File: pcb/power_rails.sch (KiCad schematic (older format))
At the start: 26 parts

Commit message: worked on configuration
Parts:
- removed C? (x2): 4.7uF, symbol C
- removed U?: TLV702xx-DBV, symbol TLV702xx-DBV
- added C? (x2): 47uF, symbol C
- added C?: 10uF, symbol C
- added C? (x2): DNP, symbol C
- added C? (x2): 150uF, symbol CP1
- added C?: C, symbol C
- added CON?: BARREL_JACK, symbol BARREL_JACK
- added F?: FUSE, symbol FUSE
- added R?: 13.3K, symbol R
- added R?: 8.25K, symbol R
- added R?: 215K, symbol R
- added U?: LTM4622, symbol LTM4622
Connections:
- net labels added: +12V
- wire segments 90 -> 129
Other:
- note added: "Channel 1: 3.3V\nChannel 2: 5V"
- note removed: "3V3 For Misc."
- moved on the sheet: C?, R?

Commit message: schematic completed. Time for review
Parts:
- removed C?: 0.47uF, symbol C
- removed C?: 22uF, symbol C
- removed C? (x2): 4.7uF, symbol C
- removed R? (x2): 10K, symbol R
- removed U?: XRP2997, symbol XRP2997
- added FB?: FILTER, symbol FILTER
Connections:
- net labels removed: VTT
- wire segments 129 -> 109
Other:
- note removed: "DDR VTT Regulator"
- moved on the sheet: C?, U?

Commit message: Added part numbers and updated schematic
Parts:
- gave numbers to parts that had none: 31

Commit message: mostly done with component placement
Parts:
- removed C310, C311: 150uF, symbol CP1
- added C310, C311: 47uF, wbraun_smd:C_0805, symbol C
- C301, C302, C303, C312, C313, C314, C315: footprint (none) -> wbraun_smd:C_0402
- C304, C305, C306, C307, C308, C309: footprint (none) -> wbraun_smd:C_0805
- C316: value C -> 10uF; footprint (none) -> wbraun_smd:C_0805
- CON301: footprint (none) -> wbraun_smd:DC_2.1mm_PJ-202A
- F301: footprint (none) -> wbraun_smd:SMD-0805
- FB301: footprint (none) -> wbraun_smd:L_0603
- R301, R302, R303, R304, R305, R306, R307, R308: footprint (none) -> wbraun_smd:R_0402
- U301, U302: footprint (none) -> wbraun_smd:LGA25_6_25x6_25
- U303: footprint (none) -> wbraun_smd:TSOT-23-5
- U304: footprint (none) -> wbraun_smd:SOT223-5
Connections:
- net +3V3: now also C310.1
- net +5V: now also C311.1
- net GND: now also C310.2, C311.2
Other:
- note added: "10uF decoupling caps are 0805"
- note added: "47uF are 0805"

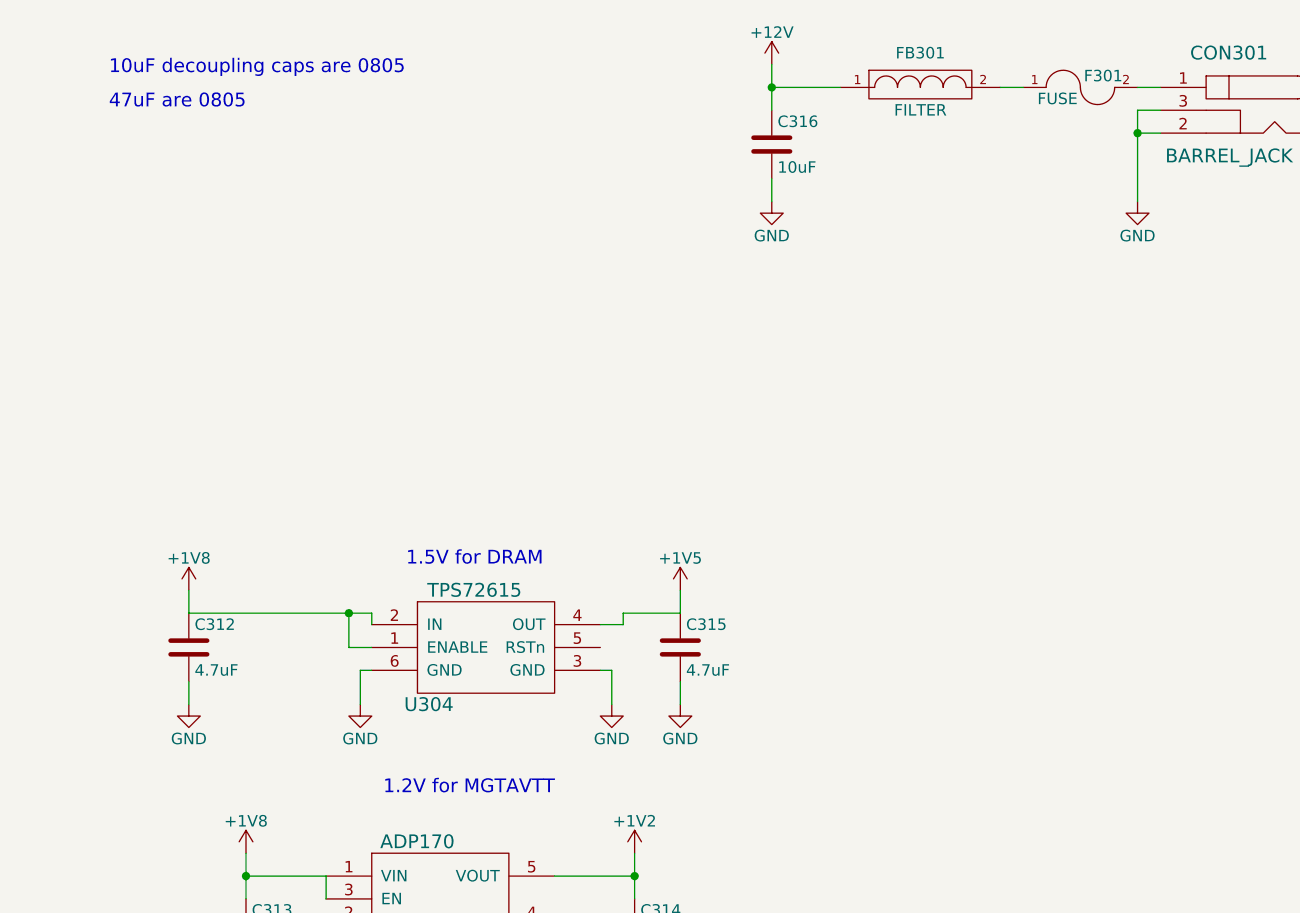
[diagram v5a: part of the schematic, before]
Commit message: Finished most of the routing, removed DDR-3
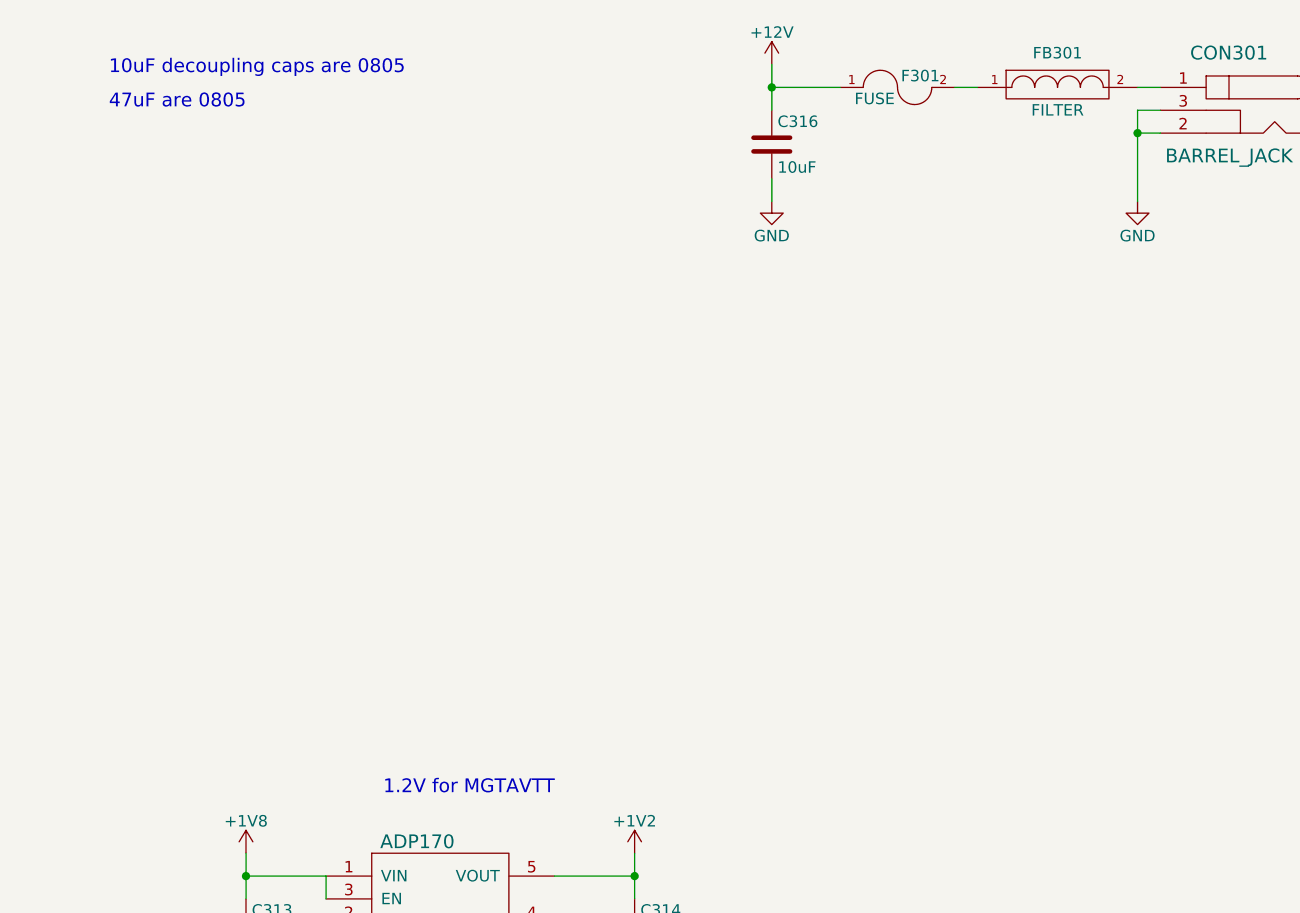
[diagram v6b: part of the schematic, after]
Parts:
- removed C312, C315: 4.7uF, wbraun_smd:C_0402, symbol C
- removed U304: TPS72615, wbraun_smd:SOT223-5, symbol TPS72615
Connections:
- net +12V: now also F301.1; no longer FB301.1
- net at CON301.1: now also FB301.2; no longer F301.2
- new net: F301.2, FB301.1
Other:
- note removed: "1.5V for DRAM"
- moved on the sheet: F301, FB301
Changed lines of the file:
@@
 $Descr A4 11693 8268
 encoding utf-8
-Sheet 3 13
+Sheet 3 11
 Title ""
 Date ""
@@
 1V @ 0.15A for MGTAVCC
 $Comp
-L TPS72615 U304
-U 1 1 561AB60E
-P 6850 3450
-F 0 "U304" H 6600 3200 60  0000 C CNN
-F 1 "TPS72615" H 6800 3700 60  0000 C CNN
-F 2 "wbraun_smd:SOT223-5" H 7450 3250 60  0001 C CNN
-F 3 "" H 7450 3250 60  0000 C CNN
-	1    6850 3450
-	1    0    0    -1
-$EndComp
-$Comp
 L ADP170 U303
 U 1 1 561AB8F7
@@
 F 3 "" H 4200 1350 60  0000 C CNN
 	1    4200 1350
-	1    0    0    -1
-$EndComp
-$Comp
-L C C312
-U 1 1 561AD736
-P 5550 3450
-F 0 "C312" H 5575 3550 50  0000 L CNN
-F 1 "4.7uF" H 5575 3350 50  0000 L CNN
-F 2 "wbraun_smd:C_0402" H 5588 3300 30  0001 C CNN
-F 3 "" H 5550 3450 60  0000 C CNN
-	1    5550 3450
-	1    0    0    -1
-$EndComp
-$Comp
-L C C315
-U 1 1 561AD79D
-P 7700 3450
-F 0 "C315" H 7725 3550 50  0000 L CNN
-F 1 "4.7uF" H 7725 3350 50  0000 L CNN
-F 2 "wbraun_smd:C_0402" H 7738 3300 30  0001 C CNN
-F 3 "" H 7700 3450 60  0000 C CNN
-	1    7700 3450
 	1    0    0    -1
 $EndComp
@@
 Wire Wire Line
 	1750 1550 1750 1600
-Text Notes 6500 3100 0    60   ~ 0
-1.5V for DRAM
-Wire Wire Line
-	6350 3450 6250 3450
 Text Label 1650 2150 2    60   ~ 0
 1V8_PGOOD
 Connection ~ 1750 2150
-Wire Wire Line
-	5550 3300 6350 3300
-Wire Wire Line
-	6350 3300 6350 3350
-$Comp
-L GND #PWR024
-U 1 1 561AF8D8
-P 5550 3700
-F 0 "#PWR024" H 5550 3450 50  0001 C CNN
-F 1 "GND" H 5550 3550 50  0000 C CNN
-F 2 "" H 5550 3700 60  0000 C CNN
-F 3 "" H 5550 3700 60  0000 C CNN
-	1    5550 3700
-	1    0    0    -1
-$EndComp
-$Comp
-L GND #PWR025
-U 1 1 561AF912
-P 6300 3700
-F 0 "#PWR025" H 6300 3450 50  0001 C CNN
-F 1 "GND" H 6300 3550 50  0000 C CNN
-F 2 "" H 6300 3700 60  0000 C CNN
-F 3 "" H 6300 3700 60  0000 C CNN
-	1    6300 3700
-	1    0    0    -1
-$EndComp
-$Comp
-L GND #PWR026
-U 1 1 561AF94C
-P 7400 3700
-F 0 "#PWR026" H 7400 3450 50  0001 C CNN
-F 1 "GND" H 7400 3550 50  0000 C CNN
-F 2 "" H 7400 3700 60  0000 C CNN
-F 3 "" H 7400 3700 60  0000 C CNN
-	1    7400 3700
-	1    0    0    -1
-$EndComp
-Wire Wire Line
-	6350 3550 6300 3550
-Wire Wire Line
-	6300 3550 6300 3700
-Wire Wire Line
-	5550 3600 5550 3700
-Wire Wire Line
-	7350 3350 7450 3350
-Wire Wire Line
-	7450 3350 7450 3300
-Wire Wire Line
-	7450 3300 7700 3300
-Wire Wire Line
-	7350 3550 7400 3550
-Wire Wire Line
-	7400 3550 7400 3700
-$Comp
-L GND #PWR027
-U 1 1 561AFACB
-P 7700 3700
-F 0 "#PWR027" H 7700 3450 50  0001 C CNN
-F 1 "GND" H 7700 3550 50  0000 C CNN
-F 2 "" H 7700 3700 60  0000 C CNN
-F 3 "" H 7700 3700 60  0000 C CNN
-	1    7700 3700
-	1    0    0    -1
-$EndComp
-Wire Wire Line
-	7700 3600 7700 3700
-$Comp
-L +1V8 #PWR028
-U 1 1 561AFBAC
-P 5550 3200
-F 0 "#PWR028" H 5550 3050 50  0001 C CNN
-F 1 "+1V8" H 5550 3340 50  0000 C CNN
-F 2 "" H 5550 3200 60  0000 C CNN
-F 3 "" H 5550 3200 60  0000 C CNN
-	1    5550 3200
-	1    0    0    -1
-$EndComp
-$Comp
-L +1V5 #PWR029
-U 1 1 561AFBE6
-P 7700 3200
-F 0 "#PWR029" H 7700 3050 50  0001 C CNN
-F 1 "+1V5" H 7700 3340 50  0000 C CNN
-F 2 "" H 7700 3200 60  0000 C CNN
-F 3 "" H 7700 3200 60  0000 C CNN
-	1    7700 3200
-	1    0    0    -1
-$EndComp
-Wire Wire Line
-	7700 3300 7700 3200
-Wire Wire Line
-	5550 3200 5550 3300
 Text Notes 6400 4100 0    60   ~ 0
 1.2V for MGTAVTT
@@
 L FUSE F301
 U 1 1 563456FC
-P 9450 1000
-F 0 "F301" H 9550 1050 50  0000 C CNN
-F 1 "FUSE" H 9350 950 50  0000 C CNN
-F 2 "wbraun_smd:SMD-0805" H 9450 1000 60  0001 C CNN
-F 3 "" H 9450 1000 60  0000 C CNN
-	1    9450 1000
+P 8650 1000
+F 0 "F301" H 8750 1050 50  0000 C CNN
+F 1 "FUSE" H 8550 950 50  0000 C CNN
+F 2 "wbraun_smd:SMD-0805" H 8650 1000 60  0001 C CNN
+F 3 "" H 8650 1000 60  0000 C CNN
+	1    8650 1000
 	1    0    0    -1
 $EndComp
@@
 Wire Wire Line
 	8100 1400 8100 1500
-Wire Wire Line
-	6250 3450 6250 3300
-Connection ~ 6250 3300
 $Comp
 L FILTER FB301
 U 1 1 56537CA5
-P 8750 1000
-F 0 "FB301" H 8750 1150 50  0000 C CNN
-F 1 "FILTER" H 8750 900 50  0000 C CNN
-F 2 "wbraun_smd:L_0603" H 8750 1000 60  0001 C CNN
-F 3 "" H 8750 1000 60  0000 C CNN
-	1    8750 1000
-	1    0    0    -1
-$EndComp
-Wire Wire Line
-	9200 1000 9100 1000
+P 9350 1000
+F 0 "FB301" H 9350 1150 50  0000 C CNN
+F 1 "FILTER" H 9350 900 50  0000 C CNN
+F 2 "wbraun_smd:L_0603" H 9350 1000 60  0001 C CNN
+F 3 "" H 9350 1000 60  0000 C CNN
+	1    9350 1000
+	1    0    0    -1
+$EndComp
 Text Notes 5200 950  0    60   ~ 0
 10uF decoupling caps are 0805
@@
 	1    0    0    -1
 $EndComp
+Wire Wire Line
+	9000 1000 8900 1000
 $EndSCHEMATC

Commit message: power routing finished
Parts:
- R304: value 13.3K -> 8.25K
- R308: value 8.25K -> 13.3K
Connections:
- net +3V3: now also C309.1, C311.1, U302.A1 (VOUT2), U302.B1 (VOUT2); no longer C308.1, C310.1, U302.D1 (VOUT1), U302.E1 (VOUT1)
- net +5V: now also C308.1, C310.1, U302.D1 (VOUT1), U302.E1 (VOUT1); no longer C309.1, C311.1, U302.A1 (VOUT2), U302.B1 (VOUT2)
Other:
- note added: "Channel 2: 3.3V\nChannel 1: 5V"
- note removed: "Channel 1: 3.3V\nChannel 2: 5V"
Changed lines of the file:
@@
 	6150 4550 6150 4450
 $Comp
-L +1V8 #PWR030
+L +1V8 #PWR024
 U 1 1 561B0526
 P 5800 4350
-F 0 "#PWR030" H 5800 4200 50  0001 C CNN
+F 0 "#PWR024" H 5800 4200 50  0001 C CNN
 F 1 "+1V8" H 5800 4490 50  0000 C CNN
 F 2 "" H 5800 4350 60  0000 C CNN
@@
 $EndComp
 $Comp
-L +1V2 #PWR031
+L +1V2 #PWR025
 U 1 1 561B0560
 P 7500 4350
-F 0 "#PWR031" H 7500 4200 50  0001 C CNN
+F 0 "#PWR025" H 7500 4200 50  0001 C CNN
 F 1 "+1V2" H 7500 4490 50  0000 C CNN
 F 2 "" H 7500 4350 60  0000 C CNN
@@
 $EndComp
 $Comp
-L GND #PWR032
+L GND #PWR026
 U 1 1 561B059A
 P 6150 4950
-F 0 "#PWR032" H 6150 4700 50  0001 C CNN
+F 0 "#PWR026" H 6150 4700 50  0001 C CNN
 F 1 "GND" H 6150 4800 50  0000 C CNN
 F 2 "" H 6150 4950 60  0000 C CNN
@@
 $EndComp
 $Comp
-L GND #PWR033
+L GND #PWR027
 U 1 1 561B05D4
 P 7500 4950
-F 0 "#PWR033" H 7500 4700 50  0001 C CNN
+F 0 "#PWR027" H 7500 4700 50  0001 C CNN
 F 1 "GND" H 7500 4800 50  0000 C CNN
 F 2 "" H 7500 4950 60  0000 C CNN
@@
 $EndComp
 $Comp
-L GND #PWR034
+L GND #PWR028
 U 1 1 561B060E
 P 5800 4950
-F 0 "#PWR034" H 5800 4700 50  0001 C CNN
+F 0 "#PWR028" H 5800 4700 50  0001 C CNN
 F 1 "GND" H 5800 4800 50  0000 C CNN
 F 2 "" H 5800 4950 60  0000 C CNN
@@
 $EndComp
 $Comp
-L GND #PWR035
+L GND #PWR029
 U 1 1 563433E8
 P 4000 6250
-F 0 "#PWR035" H 4000 6000 50  0001 C CNN
+F 0 "#PWR029" H 4000 6000 50  0001 C CNN
 F 1 "GND" H 4000 6100 50  0000 C CNN
 F 2 "" H 4000 6250 60  0000 C CNN
@@
 $EndComp
 $Comp
-L GND #PWR036
+L GND #PWR030
 U 1 1 563433EE
 P 2200 4700
-F 0 "#PWR036" H 2200 4450 50  0001 C CNN
+F 0 "#PWR030" H 2200 4450 50  0001 C CNN
 F 1 "GND" H 2200 4550 50  0000 C CNN
 F 2 "" H 2200 4700 60  0000 C CNN
@@
 P 1900 6350
 F 0 "R304" H 2150 6400 50  0000 C CNN
-F 1 "13.3K" H 2100 6300 50  0000 C CNN
+F 1 "8.25K" H 2100 6300 50  0000 C CNN
 F 2 "wbraun_smd:R_0402" V 1830 6350 30  0001 C CNN
 F 3 "" H 1900 6350 30  0000 C CNN
@@
 P 2200 6350
 F 0 "R308" H 2100 6400 50  0000 C CNN
-F 1 "8.25K" H 2050 6300 50  0000 C CNN
+F 1 "13.3K" H 2200 6300 50  0000 C CNN
 F 2 "wbraun_smd:R_0402" V 2130 6350 30  0001 C CNN
 F 3 "" H 2200 6350 30  0000 C CNN
@@
 $EndComp
 Text Notes 2700 4050 0    60   ~ 0
-Channel 1: 3.3V\nChannel 2: 5V
+Channel 2: 3.3V\nChannel 1: 5V
 Wire Wire Line
 	2400 6200 2200 6200
@@
 	1900 6100 1900 6200
 $Comp
-L GND #PWR037
+L GND #PWR031
 U 1 1 56343416
 P 1900 6600
-F 0 "#PWR037" H 1900 6350 50  0001 C CNN
+F 0 "#PWR031" H 1900 6350 50  0001 C CNN
 F 1 "GND" H 1900 6450 50  0000 C CNN
 F 2 "" H 1900 6600 60  0000 C CNN
@@
 $EndComp
 $Comp
-L GND #PWR038
+L GND #PWR032
 U 1 1 5634341C
 P 2200 6600
-F 0 "#PWR038" H 2200 6350 50  0001 C CNN
+F 0 "#PWR032" H 2200 6350 50  0001 C CNN
 F 1 "GND" H 2200 6450 50  0000 C CNN
 F 2 "" H 2200 6600 60  0000 C CNN
@@
 	3800 4950 3800 5100
 $Comp
-L GND #PWR039
+L GND #PWR033
 U 1 1 56343431
 P 4200 5250
-F 0 "#PWR039" H 4200 5000 50  0001 C CNN
+F 0 "#PWR033" H 4200 5000 50  0001 C CNN
 F 1 "GND" H 4100 5250 50  0000 C CNN
 F 2 "" H 4200 5250 60  0000 C CNN
@@
 $EndComp
 $Comp
-L GND #PWR040
+L GND #PWR034
 U 1 1 56343437
 P 4200 5800
-F 0 "#PWR040" H 4200 5550 50  0001 C CNN
+F 0 "#PWR034" H 4200 5550 50  0001 C CNN
 F 1 "GND" H 4200 5650 50  0000 C CNN
 F 2 "" H 4200 5800 60  0000 C CNN
@@
 Connection ~ 3800 4600
 $Comp
-L GND #PWR041
+L GND #PWR035
 U 1 1 56343449
 P 4200 4700
-F 0 "#PWR041" H 4200 4450 50  0001 C CNN
+F 0 "#PWR035" H 4200 4450 50  0001 C CNN
 F 1 "GND" H 4050 4650 50  0000 C CNN
 F 2 "" H 4200 4700 60  0000 C CNN
@@
 	4200 4700 4200 4650
 $Comp
-L GND #PWR042
+L GND #PWR036
 U 1 1 5634347E
 P 1600 6000
-F 0 "#PWR042" H 1600 5750 50  0001 C CNN
+F 0 "#PWR036" H 1600 5750 50  0001 C CNN
 F 1 "GND" H 1600 5850 50  0000 C CNN
 F 2 "" H 1600 6000 60  0000 C CNN
@@
 	2400 4700 2200 4700
 $Comp
-L +12V #PWR043
+L +12V #PWR037
 U 1 1 5634368C
 P 4200 4250
-F 0 "#PWR043" H 4200 4100 50  0001 C CNN
+F 0 "#PWR037" H 4200 4100 50  0001 C CNN
 F 1 "+12V" H 4200 4390 50  0000 C CNN
 F 2 "" H 4200 4250 60  0000 C CNN
@@
 $EndComp
 $Comp
-L +12V #PWR044
+L +12V #PWR038
 U 1 1 563436E2
 P 4200 1100
-F 0 "#PWR044" H 4200 950 50  0001 C CNN
+F 0 "#PWR038" H 4200 950 50  0001 C CNN
 F 1 "+12V" H 4200 1240 50  0000 C CNN
 F 2 "" H 4200 1100 60  0000 C CNN
@@
 $EndComp
 $Comp
-L GND #PWR045
+L GND #PWR039
 U 1 1 56343B74
 P 1800 4700
-F 0 "#PWR045" H 1800 4450 50  0001 C CNN
+F 0 "#PWR039" H 1800 4450 50  0001 C CNN
 F 1 "GND" H 1800 4550 50  0000 C CNN
 F 2 "" H 1800 4700 60  0000 C CNN
@@
 	1600 5900 1600 6000
 $Comp
-L +5V #PWR046
+L +5V #PWR040
 U 1 1 56344628
+P 4450 4900
+F 0 "#PWR040" H 4450 4750 50  0001 C CNN
+F 1 "+5V" H 4450 5040 50  0000 C CNN
+F 2 "" H 4450 4900 60  0000 C CNN
+F 3 "" H 4450 4900 60  0000 C CNN
+	1    4450 4900
+	1    0    0    -1
+$EndComp
+$Comp
+L +3V3 #PWR041
+U 1 1 563446F0
 P 4450 5450
-F 0 "#PWR046" H 4450 5300 50  0001 C CNN
-F 1 "+5V" H 4450 5590 50  0000 C CNN
+F 0 "#PWR041" H 4450 5300 50  0001 C CNN
+F 1 "+3V3" H 4450 5590 50  0000 C CNN
 F 2 "" H 4450 5450 60  0000 C CNN
 F 3 "" H 4450 5450 60  0000 C CNN
@@
 $EndComp
 $Comp
-L +3V3 #PWR047
-U 1 1 563446F0
-P 4450 4900
-F 0 "#PWR047" H 4450 4750 50  0001 C CNN
-F 1 "+3V3" H 4450 5040 50  0000 C CNN
-F 2 "" H 4450 4900 60  0000 C CNN
-F 3 "" H 4450 4900 60  0000 C CNN
-	1    4450 4900
-	1    0    0    -1
-$EndComp
-$Comp
-L +12V #PWR048
+L +12V #PWR042
 U 1 1 563448C6
 P 2300 1850
-F 0 "#PWR048" H 2300 1700 50  0001 C CNN
+F 0 "#PWR042" H 2300 1700 50  0001 C CNN
 F 1 "+12V" H 2300 1990 50  0000 C CNN
 F 2 "" H 2300 1850 60  0000 C CNN
@@
 $EndComp
 $Comp
-L +12V #PWR049
+L +12V #PWR043
 U 1 1 563458AE
 P 8100 900
-F 0 "#PWR049" H 8100 750 50  0001 C CNN
+F 0 "#PWR043" H 8100 750 50  0001 C CNN
 F 1 "+12V" H 8100 1040 50  0000 C CNN
 F 2 "" H 8100 900 60  0000 C CNN
@@
 $EndComp
 $Comp
-L GND #PWR050
+L GND #PWR044
 U 1 1 5634590C
 P 8100 1500
-F 0 "#PWR050" H 8100 1250 50  0001 C CNN
+F 0 "#PWR044" H 8100 1250 50  0001 C CNN
 F 1 "GND" H 8100 1350 50  0000 C CNN
 F 2 "" H 8100 1500 60  0000 C CNN
@@
 $EndComp
 $Comp
-L GND #PWR051
+L GND #PWR045
 U 1 1 5634598F
 P 9700 1500
-F 0 "#PWR051" H 9700 1250 50  0001 C CNN
+F 0 "#PWR045" H 9700 1250 50  0001 C CNN
 F 1 "GND" H 9700 1350 50  0000 C CNN
 F 2 "" H 9700 1500 60  0000 C CNN

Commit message: Pending final check
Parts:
- added C312, C315, C317, C318, C319, C320: 47uF, wbraun_smd:C_0805, symbol C
- added R309: 215K, wbraun_smd:R_0402, symbol R
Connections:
- net +1V0: now also C312.1, C319.1
- net +1V8: now also C315.1, C320.1
- net +3V3: now also C318.1
- net +5V: now also C317.1
- net GND: now also C312.2, C315.2, C317.2, C318.2, C319.2, C320.2, R309.2
- net at U301.C4 (FREQ): now also R309.1
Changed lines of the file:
@@
 	3950 2350 3950 2300
 Wire Wire Line
-	3950 2300 4450 2300
+	3950 2300 4900 2300
 Wire Wire Line
 	3800 1800 3800 1950
@@
 	3950 1800 3950 1750
 Wire Wire Line
-	3950 1750 4450 1750
+	3950 1750 4900 1750
 Connection ~ 3800 1850
 Wire Wire Line
@@
 	3950 5500 3950 5450
 Wire Wire Line
-	3950 5450 4450 5450
+	3950 5450 4750 5450
 Wire Wire Line
 	3800 4950 3800 5100
@@
 	3950 4950 3950 4900
 Wire Wire Line
-	3950 4900 4450 4900
+	3950 4900 4750 4900
 Connection ~ 3800 5000
 Wire Wire Line
@@
 	4200 4350 4200 4250
 Wire Wire Line
-	4200 5200 4450 5200
-Wire Wire Line
-	4450 5750 4200 5750
+	4200 5200 4750 5200
+Wire Wire Line
+	4200 5750 4750 5750
 $Comp
 L BARREL_JACK CON301
@@
 Wire Wire Line
 	9000 1000 8900 1000
+$Comp
+L C C315
+U 1 1 567B3FD2
+P 4600 2450
+F 0 "C315" H 4625 2550 50  0000 L CNN
+F 1 "47uF" H 4400 2350 50  0000 L CNN
+F 2 "wbraun_smd:C_0805" H 4638 2300 30  0001 C CNN
+F 3 "" H 4600 2450 60  0000 C CNN
+	1    4600 2450
+	1    0    0    -1
+$EndComp
+$Comp
+L C C312
+U 1 1 567B412D
+P 4600 1900
+F 0 "C312" H 4625 2000 50  0000 L CNN
+F 1 "47uF" H 4400 1800 50  0000 L CNN
+F 2 "wbraun_smd:C_0805" H 4638 1750 30  0001 C CNN
+F 3 "" H 4600 1900 60  0000 C CNN
+	1    4600 1900
+	1    0    0    -1
+$EndComp
+Wire Wire Line
+	4200 2050 4900 2050
+Connection ~ 4450 1750
+Connection ~ 4450 2300
+Wire Wire Line
+	4200 2600 4900 2600
+Connection ~ 4600 1750
+Connection ~ 4600 2050
+Connection ~ 4600 2300
+Connection ~ 4600 2600
+Connection ~ 4450 4900
+Connection ~ 4450 5200
+Connection ~ 4450 5450
+Connection ~ 4450 5750
+$Comp
+L C C320
+U 1 1 567B5495
+P 4900 2450
+F 0 "C320" H 4925 2550 50  0000 L CNN
+F 1 "47uF" H 4700 2350 50  0000 L CNN
+F 2 "wbraun_smd:C_0805" H 4938 2300 30  0001 C CNN
+F 3 "" H 4900 2450 60  0000 C CNN
+	1    4900 2450
+	1    0    0    -1
+$EndComp
+$Comp
+L C C319
+U 1 1 567B550C
+P 4900 1900
+F 0 "C319" H 4925 2000 50  0000 L CNN
+F 1 "47uF" H 4700 1800 50  0000 L CNN
+F 2 "wbraun_smd:C_0805" H 4938 1750 30  0001 C CNN
+F 3 "" H 4900 1900 60  0000 C CNN
+	1    4900 1900
+	1    0    0    -1
+$EndComp
+$Comp
+L C C317
+U 1 1 567B5727
+P 4750 5050
+F 0 "C317" H 4775 5150 50  0000 L CNN
+F 1 "47uF" H 4550 4950 50  0000 L CNN
+F 2 "wbraun_smd:C_0805" H 4788 4900 30  0001 C CNN
+F 3 "" H 4750 5050 60  0000 C CNN
+	1    4750 5050
+	1    0    0    -1
+$EndComp
+$Comp
+L C C318
+U 1 1 567B579F
+P 4750 5600
+F 0 "C318" H 4775 5700 50  0000 L CNN
+F 1 "47uF" H 4550 5500 50  0000 L CNN
+F 2 "wbraun_smd:C_0805" H 4788 5450 30  0001 C CNN
+F 3 "" H 4750 5600 60  0000 C CNN
+	1    4750 5600
+	1    0    0    -1
+$EndComp
+$Comp
+L R R309
+U 1 1 567B5C32
+P 2200 1450
+F 0 "R309" V 2280 1450 50  0000 C CNN
+F 1 "215K" V 2200 1450 50  0000 C CNN
+F 2 "wbraun_smd:R_0402" V 2130 1450 30  0001 C CNN
+F 3 "" H 2200 1450 30  0000 C CNN
+	1    2200 1450
+	0    1    1    0
+$EndComp
+$Comp
+L GND #PWR046
+U 1 1 567B5C38
+P 1950 1550
+F 0 "#PWR046" H 1950 1300 50  0001 C CNN
+F 1 "GND" H 1950 1400 50  0000 C CNN
+F 2 "" H 1950 1550 60  0000 C CNN
+F 3 "" H 1950 1550 60  0000 C CNN
+	1    1950 1550
+	1    0    0    -1
+$EndComp
+Wire Wire Line
+	2050 1450 1950 1450
+Wire Wire Line
+	1950 1450 1950 1550
+Wire Wire Line
+	2400 1450 2350 1450
 $EndSCHEMATC
